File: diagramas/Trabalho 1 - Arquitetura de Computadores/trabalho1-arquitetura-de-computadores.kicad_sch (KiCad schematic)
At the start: 39 parts, among them J1 Analog, J2 Digital, Q1 BC547

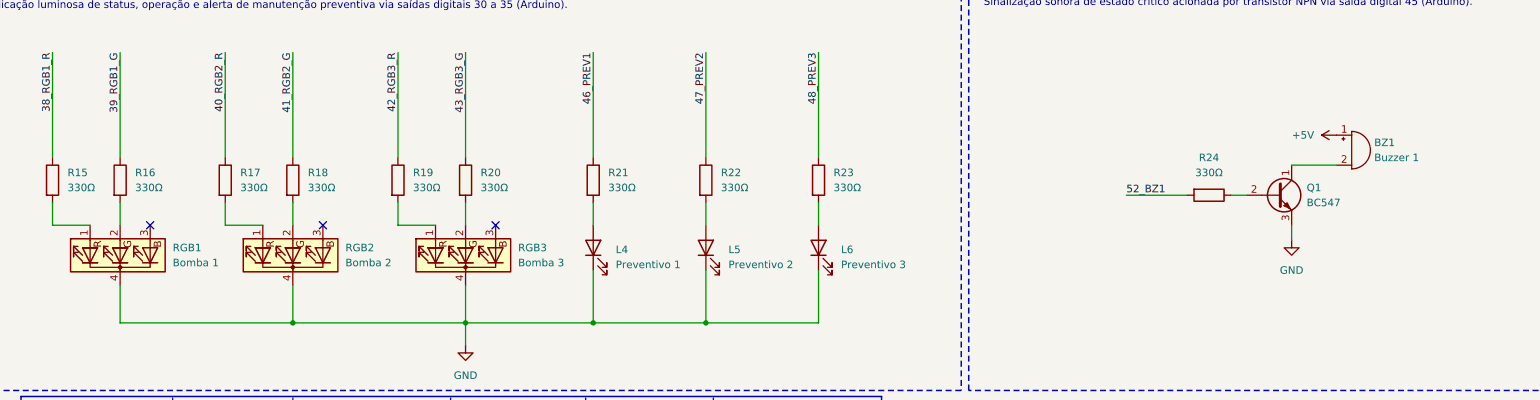
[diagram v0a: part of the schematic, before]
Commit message: trocado modelo do transistor e dos leds rgb
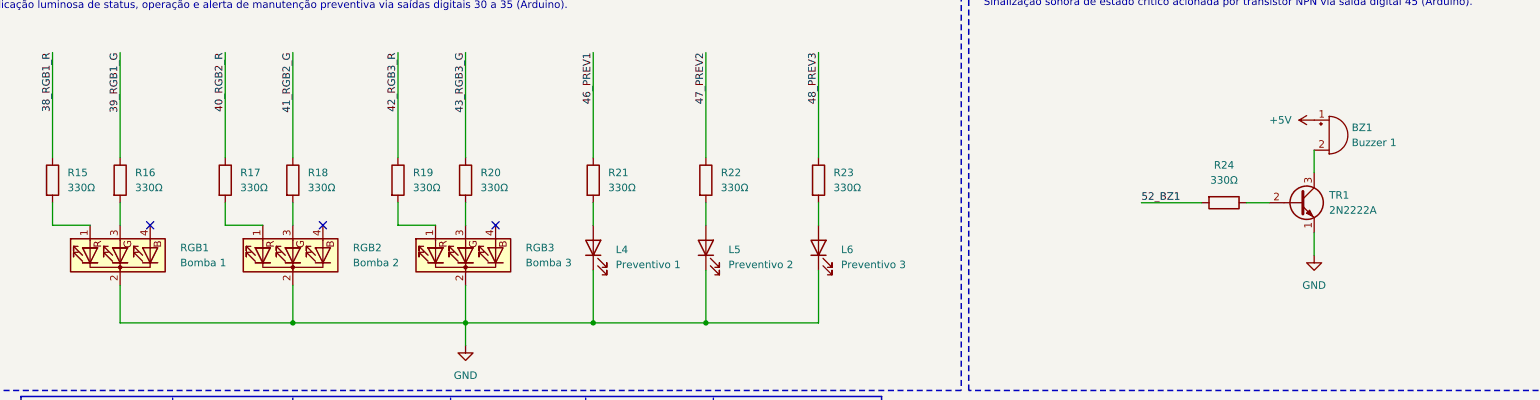
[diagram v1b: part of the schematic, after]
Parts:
- removed Q1: BC547, Package_TO_SOT_THT:TO-92_Inline, symbol Transistor_BJT:BC547
- removed RGB1: Bomba 1, LED_SMD:LED_Cree-XHP50_3V_HighDensity, symbol Device:LED_RGBK
- removed RGB2: Bomba 2, symbol Device:LED_RGBK
- removed RGB3: Bomba 3, symbol Device:LED_RGBK
- added RGB1: Bomba 1, Package_TO_SOT_THT:TO-92_Inline, symbol Device:LED_RKGB
- added RGB2: Bomba 2, symbol Device:LED_RKGB
- added RGB3: Bomba 3, symbol Device:LED_RKGB
- added TR1: 2N2222A, Package_TO_SOT_THT:TO-92_Inline, symbol Transistor_BJT:PN2222A
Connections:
- net GND: now also RGB1.2 (K), RGB2.2 (K), RGB3.2 (K), TR1.1 (E)
- net at R20.2: now also RGB3.3 (GA)
- net at R19.2: now also RGB3.1 (RA)
- net at R17.2: now also RGB2.1 (RA)
- net at R18.2: now also RGB2.3 (GA)
- net at R15.2: now also RGB1.1 (RA)
- net at R16.2: now also RGB1.3 (GA)
- net at BZ1.2 (-): now also TR1.3 (C)
- net at R24.1: now also TR1.2 (B)
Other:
- moved on the sheet: BZ1, R24

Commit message: consertados espaçamentos e textos dos módulos
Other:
- note added: "Ajuste dos parâmetros do sistema via entradas A0, A1 e A2."
- note added: "Exibição do status/número do canal ativo via saídas digitais 22 a 28 (DISP1), e 29 a 35 (DISP2)."
- note added: "Indicação luminosa de status, operação e alerta de manutenção preventiva via saídas digitais 38 a 43 (LED RGB), e 46 a 48 (LED)."
- note added: "Sinalização sonora de estado crítico acionada por transistor NPN via saída digital 52.."
- note removed: "Ajuste dos parâmetros do sistema via entradas A0, A1 e A2 (Arduino)."
- note removed: "Exibição do status/número do canal ativo via saídas digitais 22 a 28 (DISP1)"
- note removed: "Indicação luminosa de status, operação e alerta de manutenção preventiva via saídas digitais 30 a 35 (Arduino)."
- note removed: "Sinalização sonora de estado crítico acionada por transistor NPN via saída digital 45 (Arduino)."
- moved on the sheet: J2
